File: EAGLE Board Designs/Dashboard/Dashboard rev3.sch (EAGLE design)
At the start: 62 parts, among them J1 AVR-ISP-HEADER, J2 JUMPER0603, X1 CONNECTOR-6NANO-FIT_VERTICAL-6

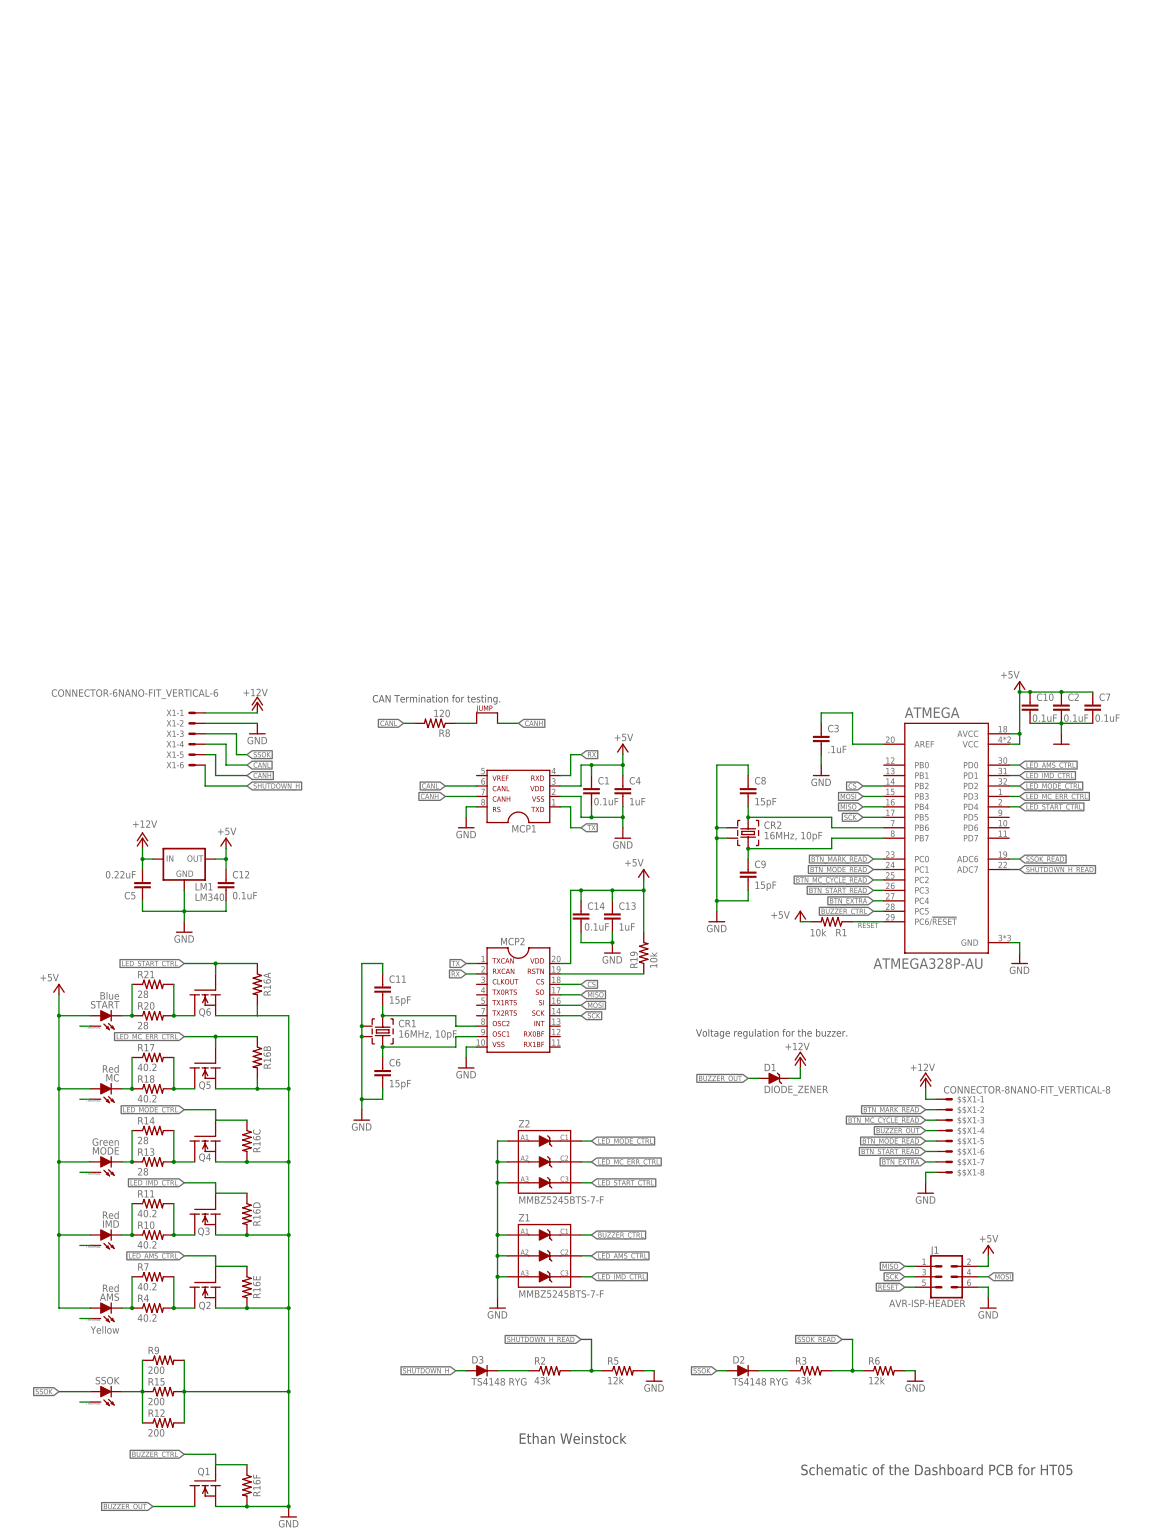
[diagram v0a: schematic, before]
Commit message: incomplete changes to schamatic for rev3 features
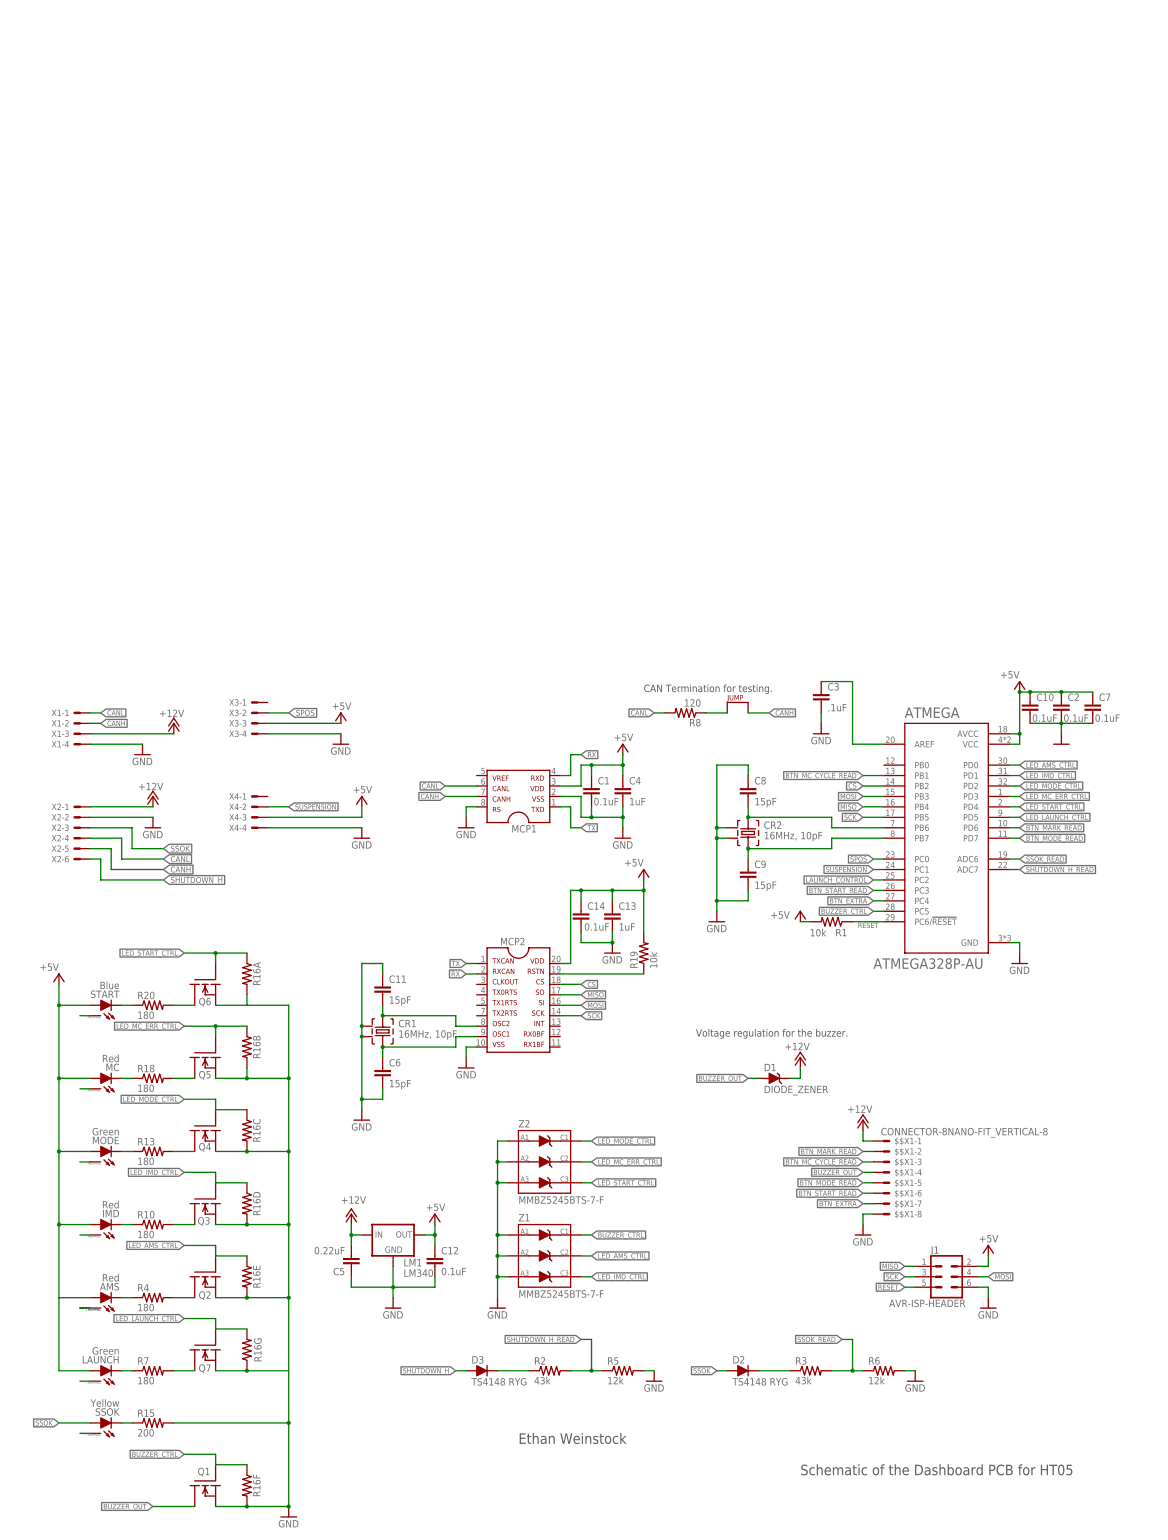
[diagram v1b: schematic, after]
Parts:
- removed R11, R17: 40.2, HyTechDevices:RESISTOR0603
- removed R12, R9: 200, HyTechDevices:RESISTOR0805-RES
- removed R14, R21: 28, HyTechDevices:RESISTOR0603
- added LAUNCH: Green, HyTechDevices:XP-E2XP-E2
- added Q7: (no value), HyTechDevices:DMG3406LSOT
- added X2: CONNECTOR-6NANO-FIT_RIGHT_ANGLE-6-SURFACE, HyTechDevices:CONNECTOR-6NANO-FIT_RIGHT_ANGLE-6-SURFACE
- added X3, X4: CONNECTOR-4NANO-FIT_RIGHT_ANGLE-4-SURFACE, HyTechDevices:CONNECTOR-4NANO-FIT_RIGHT_ANGLE-4-SURFACE
- R10, R18, R4, R7: value 40.2 -> 180
- R13, R20: value 28 -> 180
- X1: value CONNECTOR-6NANO-FIT_VERTICAL-6 -> CONNECTOR-4NANO-FIT_RIGHT_ANGLE-4-SURFACE; device HyTechDevices:CONNECTOR-6NANO-FIT_VERTICAL-6 -> HyTechDevices:CONNECTOR-4NANO-FIT_RIGHT_ANGLE-4-SURFACE
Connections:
- new net +5V1: LAUNCH.A
- new net GND1: Q7.S, R16G.1
- new net LAUNCH_CONTROL: ATMEGA.PC2
- new net LED_LAUNCH_CTRL: ATMEGA.PD5, Q7.G, R16G.2
- new net N$21: LAUNCH.C, R7.1
- new net N$22: Q7.D, R7.2
- new net SPOS: ATMEGA.PC0, X3-2.S
- new net SUSPENSION: ATMEGA.PC1, X4-2.S
- net +12V: now also X1-3.S, X2-1.S; no longer X1-1.S
- net +5V: now also X3-3.S, X4-3.S
- net BTN_MARK_READ: now also ATMEGA.PD6; no longer ATMEGA.PC0
- net BTN_MC_CYCLE_READ: now also ATMEGA.PB1; no longer ATMEGA.PC2
- net BTN_MODE_READ: now also ATMEGA.PD7; no longer ATMEGA.PC1
- net CANH: now also X1-2.S, X2-5.S; no longer X1-5.S
- net CANL: now also X1-1.S, X2-4.S; no longer X1-4.S
- net GND: now also X1-4.S, X2-2.S, X3-4.S, X4-4.S; no longer R12.2, R9.2, X1-2.S
- net N$10: no longer R14.1
- net N$11: no longer R21.1
- net N$12: no longer R14.2
- net N$13: no longer R11.1
- net N$15: no longer R12.1, R9.1
- net N$16: no longer R7.1
- net N$17: no longer R11.2
- net N$18: no longer R7.2
- net N$19: no longer R17.1
- net N$4: no longer R21.2
- net N$9: no longer R17.2
- net SHUTDOWN_H: now also X2-6.S; no longer X1-6.S
- net SSOK: now also X2-3.S; no longer X1-3.S
- net THERMAL: now also LAUNCH.X
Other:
- moved on the sheet: $$X1-1, $$X1-2, $$X1-3, $$X1-4, $$X1-5, $$X1-6, $$X1-7, $$X1-8, AMS, C12, C3, C5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

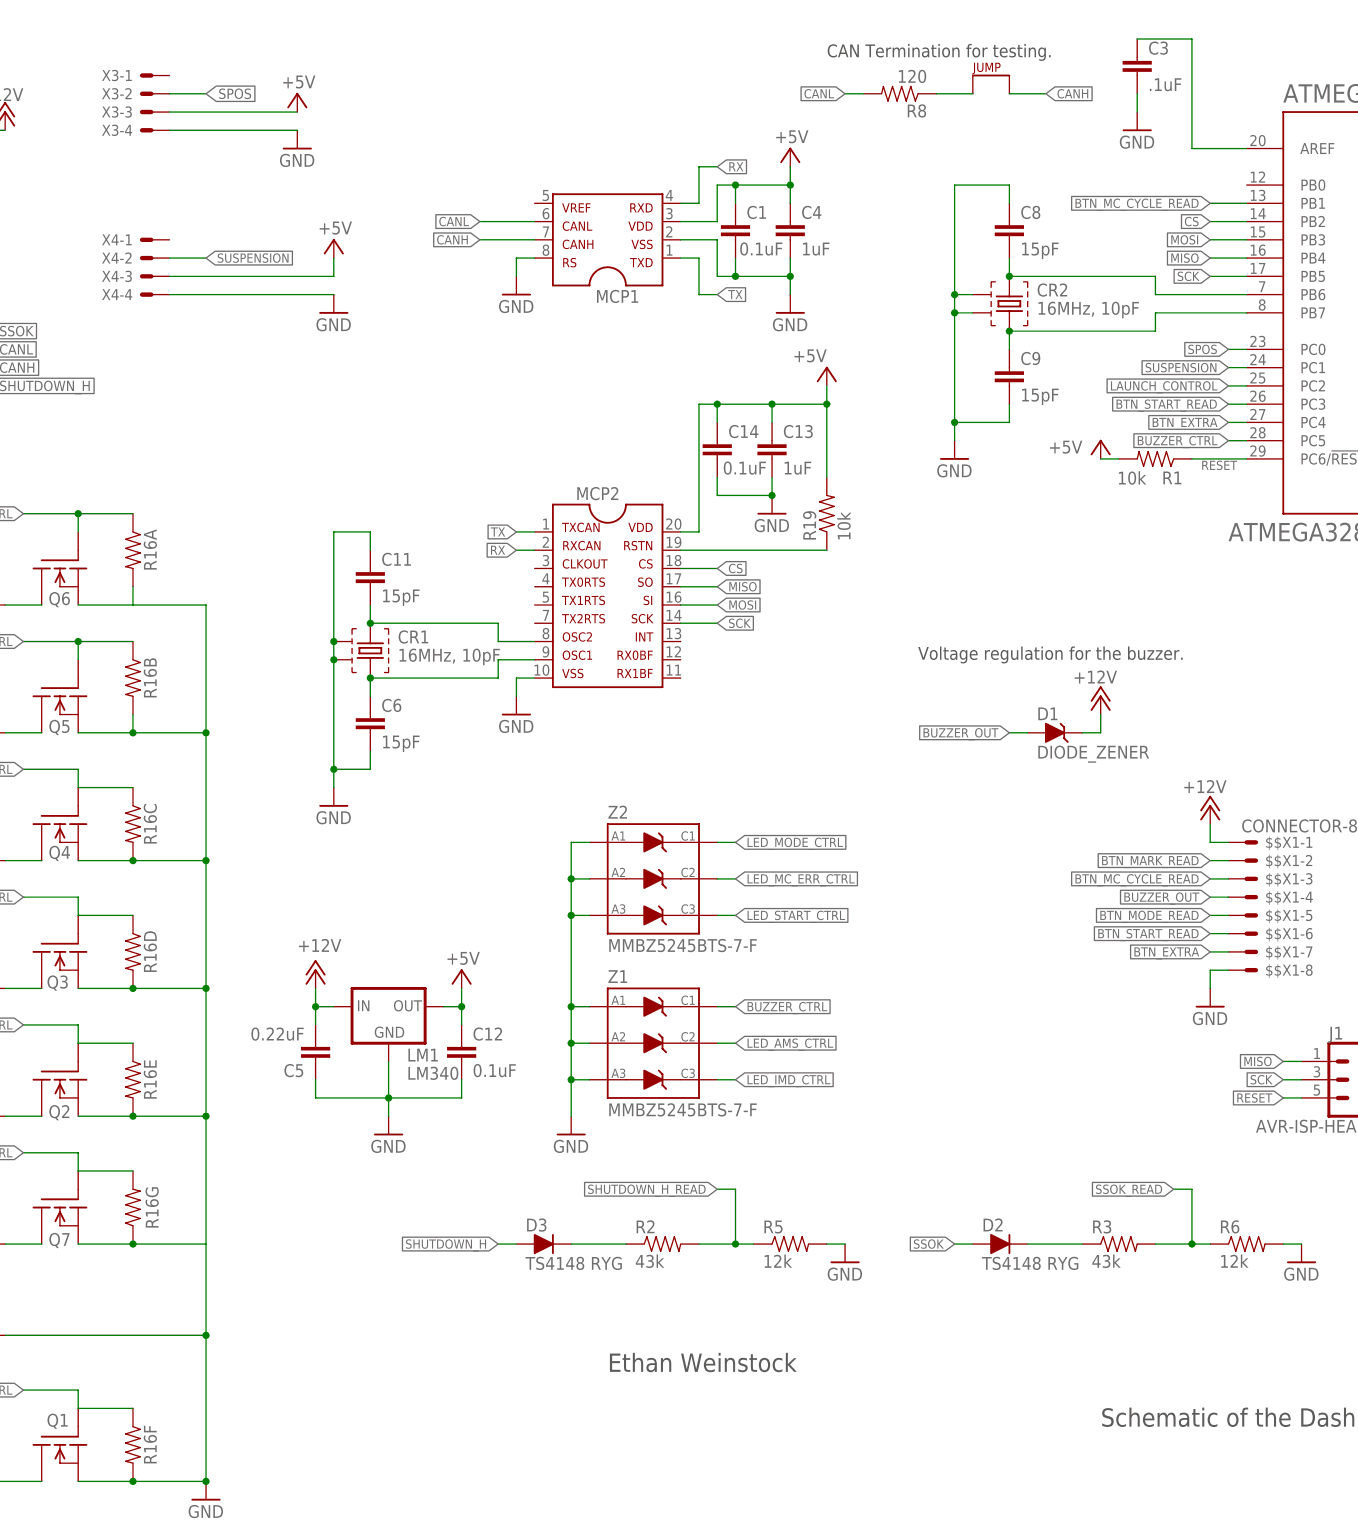
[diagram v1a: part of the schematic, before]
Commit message: Updated names to wires
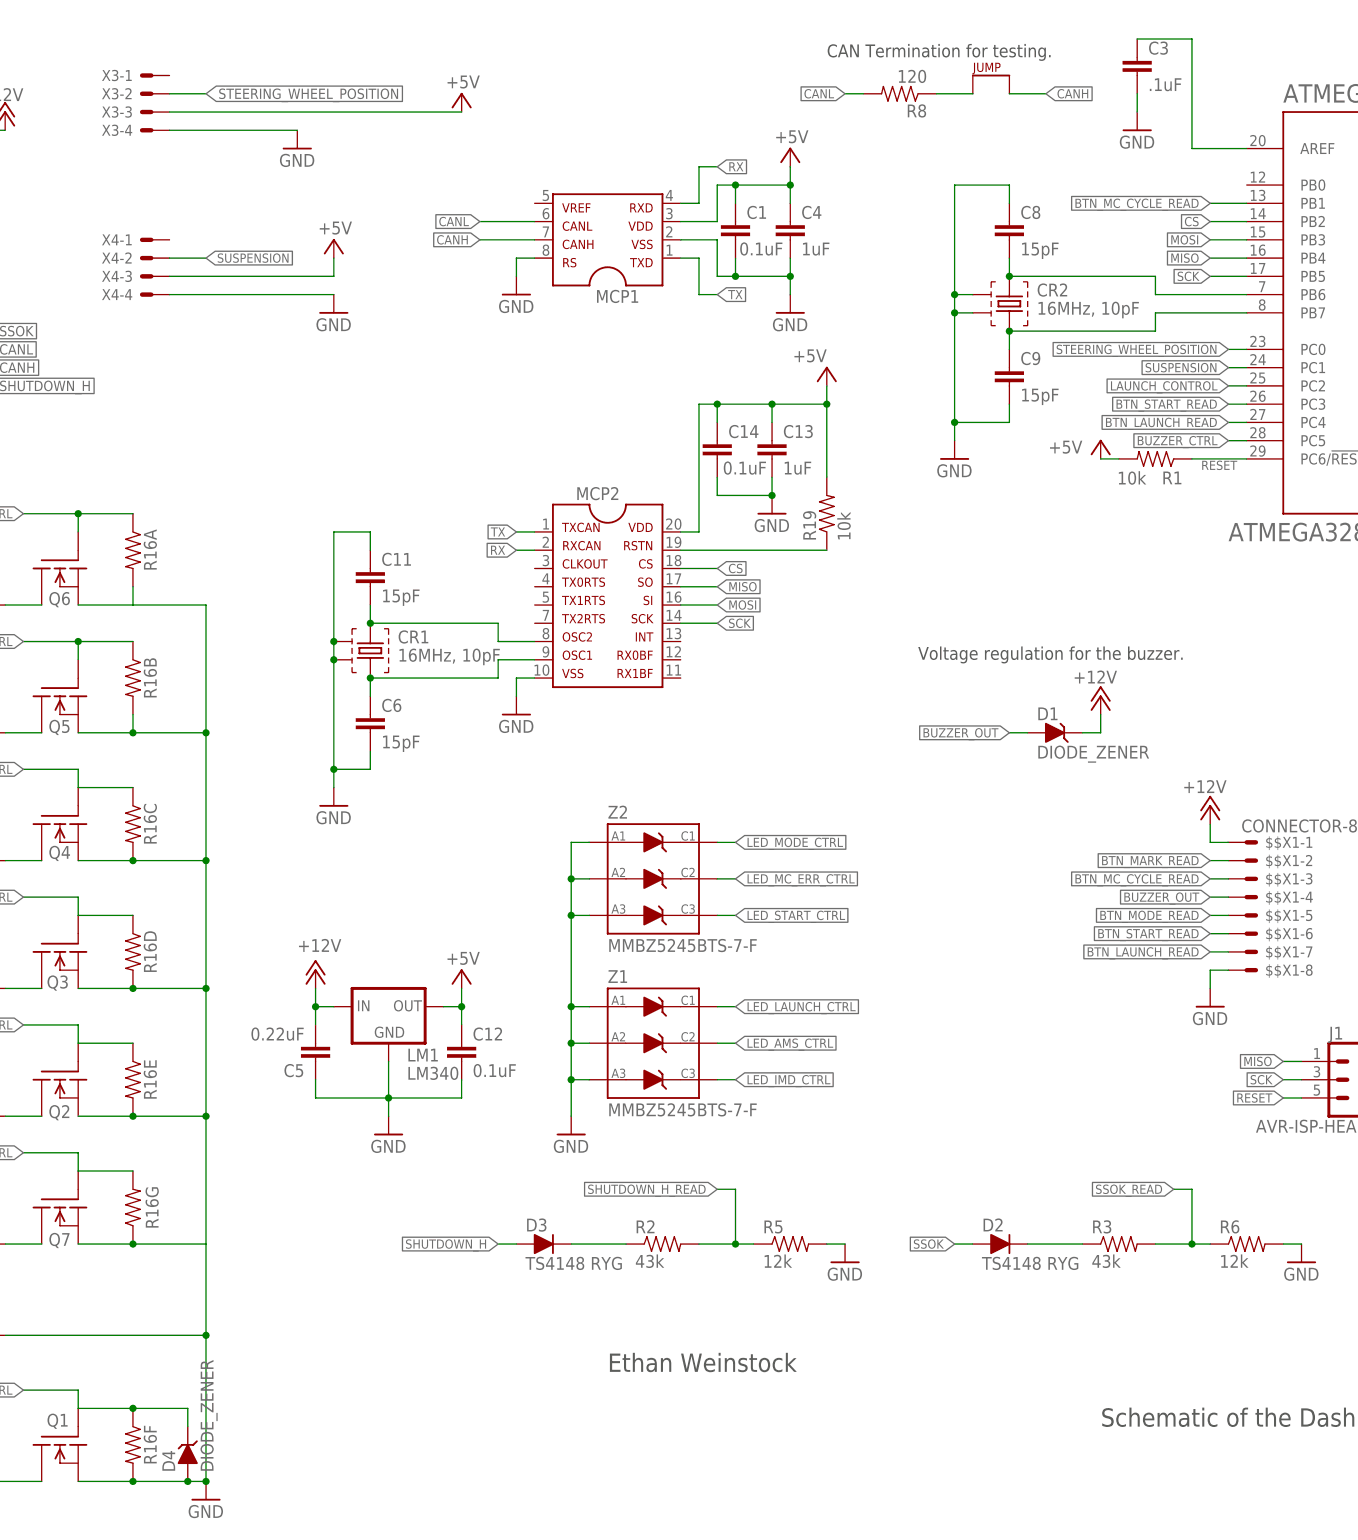
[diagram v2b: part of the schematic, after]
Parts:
- added D4: DIODE_ZENER, HyTechDevices:DIODE_ZENER
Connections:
- net BTN_EXTRA renamed BTN_LAUNCH_READ
- net SPOS renamed STEERING_WHEEL_POSITION
- net BUZZER_CTRL: now also D4.C; no longer Z1.C1
- net GND: now also D4.A
- net LED_LAUNCH_CTRL: now also Z1.C1
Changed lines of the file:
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@@
 <part name="GND20" library="HyTechSymbols" deviceset="GND" device=""/>
 <part name="P+13" library="supply1" deviceset="+5V" device=""/>
+<part name="D4" library="HyTechDevices" deviceset="DIODE_ZENER" device=""/>
 </parts>
 <sheets>
@@
 <attribute name="NAME" x="60.96" y="173.482" size="1.524" layer="95" rot="R180"/>
 </instance>
-<instance part="P+14" gate="1" x="83.82" y="200.66" smashed="yes">
-<attribute name="VALUE" x="86.36" y="203.2" size="1.778" layer="96" rot="R180"/>
+<instance part="P+14" gate="1" x="106.68" y="200.66" smashed="yes">
+<attribute name="VALUE" x="109.22" y="203.2" size="1.778" layer="96" rot="R180"/>
 </instance>
 <instance part="GND20" gate="1" x="88.9" y="170.18" smashed="yes">
@@
 <instance part="P+13" gate="1" x="88.9" y="180.34" smashed="yes">
 <attribute name="VALUE" x="91.44" y="182.88" size="1.778" layer="96" rot="R180"/>
+</instance>
+<instance part="D4" gate="G$1" x="68.58" y="12.7" smashed="yes" rot="R90">
+<attribute name="NAME" x="66.8274" y="8.89" size="1.778" layer="95" rot="R90"/>
+<attribute name="VALUE" x="72.1614" y="8.89" size="1.778" layer="96" rot="R90"/>
 </instance>
 </instances>
@@
 <segment>
 <pinref part="GND10" gate="1" pin="GND"/>
-<wire x1="71.12" y1="7.62" x2="60.96" y2="7.62" width="0.1524" layer="91"/>
+<wire x1="71.12" y1="7.62" x2="68.58" y2="7.62" width="0.1524" layer="91"/>
 <pinref part="R16" gate="F" pin="2"/>
 <junction x="60.96" y="7.62"/>
+<wire x1="68.58" y1="7.62" x2="60.96" y2="7.62" width="0.1524" layer="91"/>
 <wire x1="60.96" y1="7.62" x2="53.34" y2="7.62" width="0.1524" layer="91"/>
 <pinref part="R15" gate="G$1" pin="2"/>
@@
 <wire x1="60.96" y1="114.3" x2="60.96" y2="111.76" width="0.1524" layer="91"/>
 <junction x="60.96" y="111.76"/>
+<pinref part="D4" gate="G$1" pin="A"/>
+<junction x="68.58" y="7.62"/>
 </segment>
 <segment>
@@
 <segment>
 <pinref part="X3" gate="-3" pin="S"/>
-<wire x1="66.04" y1="198.12" x2="83.82" y2="198.12" width="0.1524" layer="91"/>
+<wire x1="66.04" y1="198.12" x2="106.68" y2="198.12" width="0.1524" layer="91"/>
 <pinref part="P+14" gate="1" pin="+5V"/>
 </segment>
@@
 <pinref part="R16" gate="F" pin="1"/>
 <wire x1="60.96" y1="17.78" x2="53.34" y2="17.78" width="0.1524" layer="91"/>
+<pinref part="D4" gate="G$1" pin="C"/>
+<wire x1="60.96" y1="17.78" x2="68.58" y2="17.78" width="0.1524" layer="91"/>
+<wire x1="68.58" y1="17.78" x2="68.58" y2="15.24" width="0.1524" layer="91"/>
+<junction x="60.96" y="17.78"/>
 </segment>
 <segment>
@@
 <wire x1="215.9" y1="152.4" x2="213.36" y2="152.4" width="0.1524" layer="91"/>
 <label x="213.36" y="152.4" size="1.27" layer="95" rot="R180" xref="yes"/>
-</segment>
-<segment>
-<pinref part="Z1" gate="G$1" pin="C1"/>
-<wire x1="142.24" y1="73.66" x2="144.78" y2="73.66" width="0.1524" layer="91"/>
-<label x="144.78" y="73.66" size="1.27" layer="95" xref="yes"/>
 </segment>
 </net>
@@
 </segment>
 </net>
-<net name="BTN_EXTRA" class="0">
+<net name="BTN_LAUNCH_READ" class="0">
 <segment>
 <pinref part="ATMEGA" gate="G$1" pin="PC4"/>
@@
 <pinref part="ATMEGA" gate="G$1" pin="PD5"/>
 </segment>
-</net>
-<net name="SPOS" class="0">
+<segment>
+<pinref part="Z1" gate="G$1" pin="C1"/>
+<wire x1="142.24" y1="73.66" x2="144.78" y2="73.66" width="0.1524" layer="91"/>
+<label x="144.78" y="73.66" size="1.27" layer="95" xref="yes"/>
+</segment>
+</net>
+<net name="STEERING_WHEEL_POSITION" class="0">
 <segment>
 <pinref part="X3" gate="-2" pin="S"/>
